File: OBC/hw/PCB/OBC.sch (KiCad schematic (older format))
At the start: 14 parts, among them J0 Raspberry_Pi_2_3, J1 Power, J11 RPI_MOUNT1, J12 RPI_MOUNT2, J13 RPI_MOUNT3, J14 RPI_MOUNT4, J2 Terminal_5V0, J3 PICOBLADE1, J4 PICOBLADE2, J5 I2C, J6 I2C, J7 CSP_I2C, J8 Power2, U0 Payload

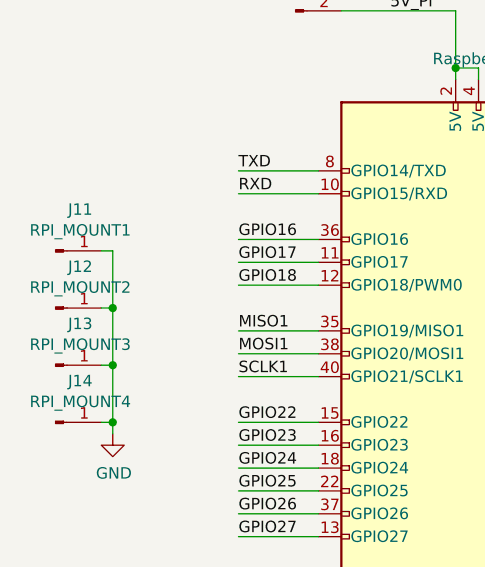
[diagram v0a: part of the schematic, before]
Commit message: Replaced pin header's footprint with the footprint of the Raspberry pi zero.
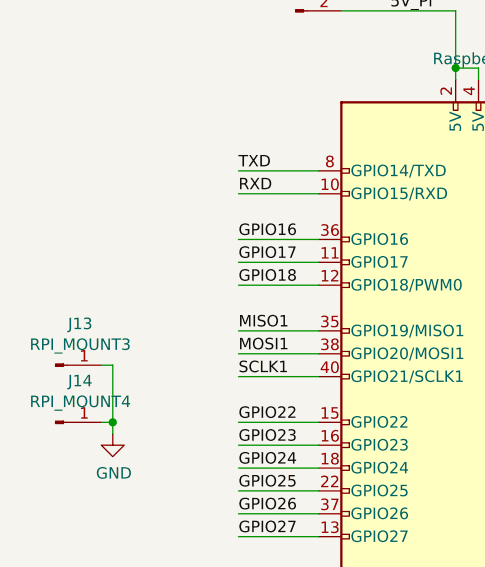
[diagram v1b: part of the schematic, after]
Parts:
- removed J11: RPI_MOUNT1, Connector_PinHeader_2.54mm:PinHeader_1x01_P2.54mm_Vertical, symbol Connector:Conn_01x01_Male
- removed J12: RPI_MOUNT2, Connector_PinHeader_2.54mm:PinHeader_1x01_P2.54mm_Vertical, symbol Connector:Conn_01x01_Male
- J0: footprint Connector_PinSocket_2.54mm:PinSocket_2x20_P2.54mm_Vertical -> Module:Raspberry_Pi_Zero_Socketed_THT_FaceDown_MountingHoles
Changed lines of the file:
@@
 F 0 "J0" H 4150 4481 50  0000 C CNN
 F 1 "Raspberry_Pi_2_3" H 4150 4390 50  0000 C CNN
-F 2 "Connector_PinSocket_2.54mm:PinSocket_2x20_P2.54mm_Vertical" H 4150 3000 50  0001 C CNN
+F 2 "Module:Raspberry_Pi_Zero_Socketed_THT_FaceDown_MountingHoles" H 4150 3000 50  0001 C CNN
 F 3 "https://www.raspberrypi.org/documentation/hardware/raspberrypi/schematics/rpi_SCH_3bplus_1p0_reduced.pdf" H 4150 3000 50  0001 C CNN
 	1    4150 3000
@@
 GND
 $Comp
-L Connector:Conn_01x01_Male J11
-U 1 1 5D290C4C
-P 2200 2450
-F 0 "J11" H 2308 2631 50  0000 C CNN
-F 1 "RPI_MOUNT1" H 2308 2540 50  0000 C CNN
-F 2 "Connector_PinHeader_2.54mm:PinHeader_1x01_P2.54mm_Vertical" H 2200 2450 50  0001 C CNN
-F 3 "~" H 2200 2450 50  0001 C CNN
-	1    2200 2450
-	1    0    0    -1
-$EndComp
-$Comp
-L Connector:Conn_01x01_Male J12
-U 1 1 5D291331
-P 2200 2700
-F 0 "J12" H 2308 2881 50  0000 C CNN
-F 1 "RPI_MOUNT2" H 2308 2790 50  0000 C CNN
-F 2 "Connector_PinHeader_2.54mm:PinHeader_1x01_P2.54mm_Vertical" H 2200 2700 50  0001 C CNN
-F 3 "~" H 2200 2700 50  0001 C CNN
-	1    2200 2700
-	1    0    0    -1
-$EndComp
-$Comp
 L Connector:Conn_01x01_Male J13
 U 1 1 5D29151A
@@
 	2450 3200 2400 3200
 Wire Wire Line
-	2400 2450 2450 2450
-Wire Wire Line
-	2450 2450 2450 2700
-Wire Wire Line
-	2400 2700 2450 2700
-Connection ~ 2450 2700
-Wire Wire Line
-	2450 2700 2450 2950
-Wire Wire Line
 	2400 2950 2450 2950
-Connection ~ 2450 2950
 Wire Wire Line
 	2450 2950 2450 3200
